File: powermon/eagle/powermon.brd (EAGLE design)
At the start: 50 x 50 mm, 42 parts, among them J1 USB, J2 USB, J3 TERMINAL-2, U1 LTC2943, U2 FT232RL, U3 LT1764AEQ, U4 ATMEGA328TQFP32

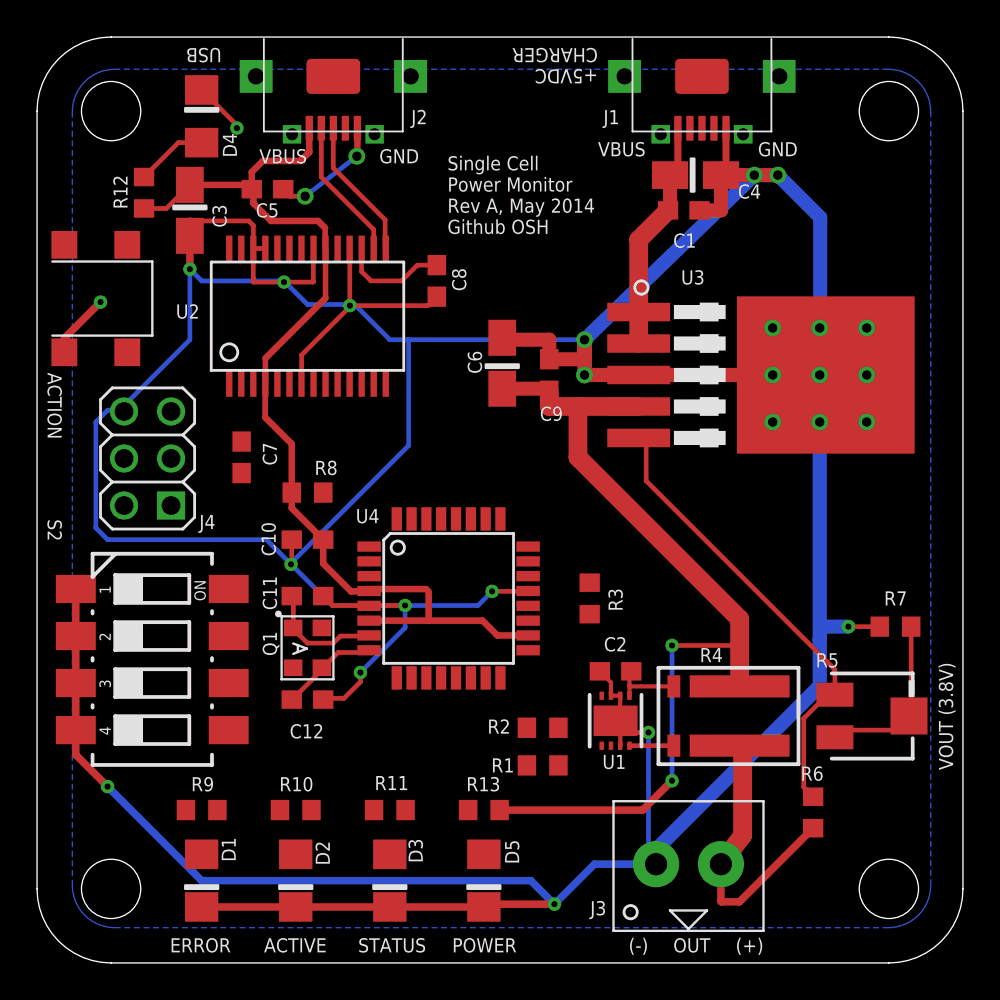
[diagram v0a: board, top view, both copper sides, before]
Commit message: Auto routed the remaining networks.
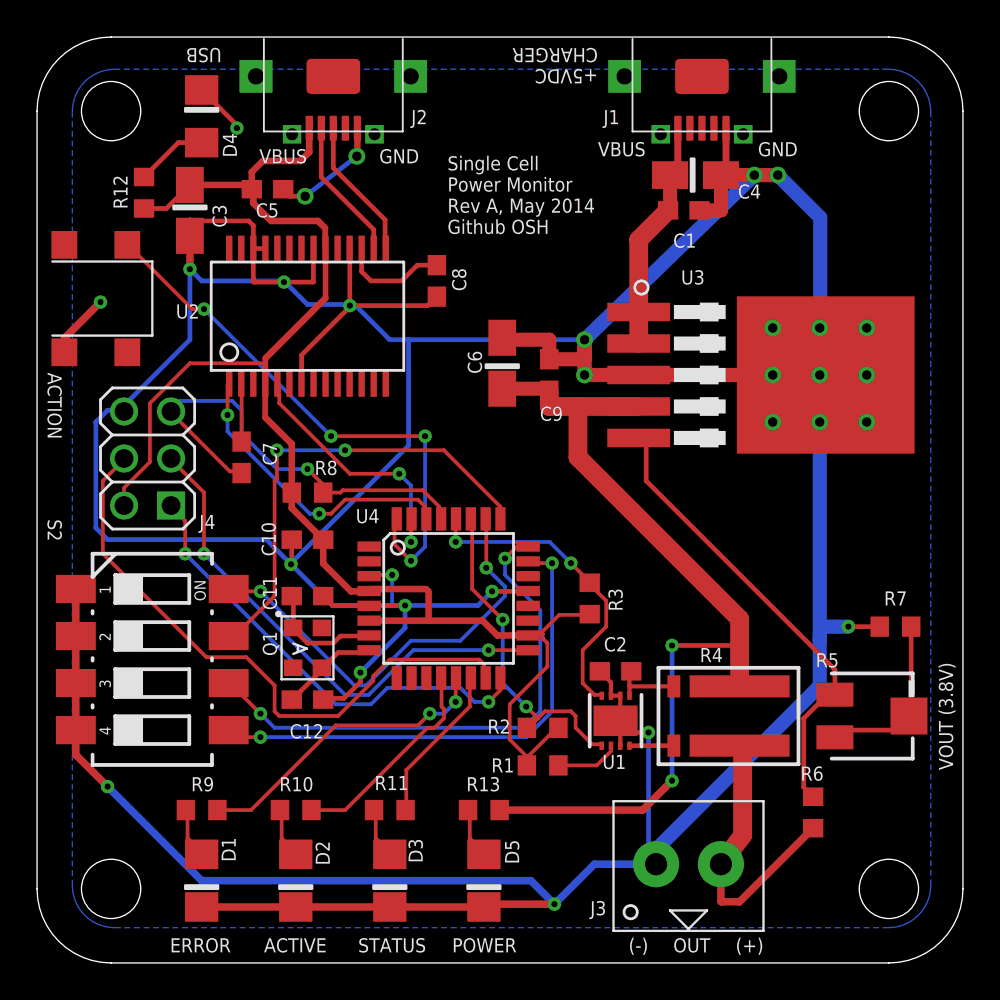
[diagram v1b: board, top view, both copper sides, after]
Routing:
- net MOSI: track 0.00 -> 32.9 mm
- net ACTION: track 0.16 -> 30.2 mm, vias 0 -> 4
- net CONFIG3: track 0.00 -> 28.7 mm, vias 0 -> 2
- net +5V: track 55.1 -> 83.6 mm
- net CONFIG4: track 0.00 -> 27.6 mm, vias 0 -> 2
- net SCK: track 0.00 -> 27.5 mm, vias 0 -> 2
- net CONFIG2: track 0.00 -> 25.3 mm, vias 0 -> 2
- net MISO: track 0.00 -> 24.9 mm, vias 0 -> 2
- net RESET: track 0.00 -> 24.3 mm, vias 0 -> 1
- net CONFIG1: track 0.00 -> 23.7 mm, vias 0 -> 2
- net I2C-DATA: track 0.00 -> 17.8 mm, vias 0 -> 2
- net I2C-CLK: track 0.10 -> 17.2 mm, vias 0 -> 2
- net ERROR_LED: track 0.21 -> 16.8 mm, vias 0 -> 2
- net SER_RX: track 0.18 -> 16.5 mm, vias 0 -> 2
- net SER_TX: track 0.00 -> 14.4 mm, vias 0 -> 2
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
